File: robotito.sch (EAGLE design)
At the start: 53 parts, among them IC1 7805T, IC2 L298, IC3 L298, J1 22-27-2031-03, J10 22-27-2031-03, J11 22-27-2031-03, J2 22-27-2031-03, J3 22-27-2031-03, J4 22-27-2031-03, J5 22-27-2031-03, J6 22-27-2031-03, J7 22-27-2031-03, J8 22-27-2031-03, J9 22-27-2031-03

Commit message: Board is routing good with ~100 vias
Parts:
- removed U$1: TEENSY_3.1-3.2_DIL+4, Teensy_3_and_LC_Series_Boards_v1.4:TEENSY_3.1-3.2_DIL+4
- added J12: 22-27-2031-03, con-molex:22-27-2031-03
- added U$2: TEENSY_3.1-3.2_ALL_PINS&PADS, Teensy_3_and_LC_Series_Boards_v1.4:TEENSY_3.1-3.2_ALL_PINS&PADS
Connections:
- removed net N$33: U$1.AGND
- removed net N$34: U$1.AREF
- removed net N$36: U$1.VUSB
- removed net N$6: U$1.2
- new net DS12: J12-1.S
- new net N$15: U$2.31/A20
- new net N$4: U$2.2
- net +3.3V: now also U$2.3.3V; no longer U$1.3.3V
- net +5V: now also J12-3.S, U$2.VIN; no longer U$1.VIN
- net DS1: now also U$2.23/A9/T/PWM; no longer U$1.15/A1/T
- net DS10: now also U$2.29/A18/SCL1; no longer U$1.A11
- net DS11: now also U$2.30/A19/SDA1; no longer U$1.A10
- net DS2: now also U$2.A10; no longer U$1.16/A2/T
- net DS3: now also U$2.A11; no longer U$1.17/A3/T
- net DS4: now also U$2.A12; no longer U$1.18/A4/T/SDA0
- net DS5: now also U$2.A13; no longer U$1.19/A5/T/SCL0
- net DS6: now also U$2.A14/DAC; no longer U$1.20/A6/PWM
- net DS7: now also U$2.26/A15; no longer U$1.21/A7/PWM
- net DS8: now also U$2.27/A16; no longer U$1.22/A8/T/PWM
- net DS9: now also U$2.28/A17; no longer U$1.23/A9/T/PWM
- net GND: now also J12-2.S, U$2.GND; no longer U$1.GND
- net M1EN: now also U$2.3/CAN-TX/PWM; no longer U$1.3/CAN-TX/PWM
- net M1ENCA: now also U$2.15/A1/T
- net M1ENCB: now also U$2.16/A2/T
- net M1I1: now also U$2.7/RX3; no longer U$1.7/RX3
- net M1I2: now also U$2.8/TX3; no longer U$1.8/TX3
- net M2EN: now also U$2.4/CAN-RX/PWM; no longer U$1.4/CAN-RX-PWM
- net M2ENCA: now also U$2.17/A3/T
- net M2ENCB: now also U$2.18/A4/T/SDA0
- net M2I1: now also U$2.9/RX2/PWM; no longer U$1.9/RX2/PWM
- net M2I2: now also U$2.10/TX2/PWM; no longer U$1.10/TX2/PWM
- net M3EN: now also U$2.5/PWM; no longer U$1.5/PWM
- net M3ENCA: now also U$2.19/A5/T/SCL0
- net M3ENCB: now also U$2.20/A6/PWM
- net M3I1: now also U$2.11/MOSI; no longer U$1.11/MOSI
- net M3I2: now also U$2.12/MISO; no longer U$1.12/MISO
- net M4EN: now also U$2.6/PWM; no longer U$1.6/PWM
- net M4ENCA: now also U$2.21/A7/PWM
- net M4ENCB: now also U$2.22/A8/T/PWM
- net M4I1: now also U$2.13/SCK/LED; no longer U$1.13/SCK/LED
- net M4I2: now also U$2.14/A0; no longer U$1.14/A0
- net RX: now also U$2.0/RX1/T; no longer U$1.0/RX1/T
- net TX: now also U$2.1/TX1/T; no longer U$1.1/TX1/T

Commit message: fixed some errors/warnings
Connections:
- removed net CTS: JP1.CTS
- removed net DIO0: JP1.DIO0
- removed net DIO1: JP1.DIO1
- removed net DIO11: JP1.DIO11
- removed net DIO12: JP1.DIO12
- removed net DIO2: JP1.DIO2
- removed net DIO3: JP1.DIO3
- removed net DIO4: JP1.DIO4
- removed net DIO9: JP1.DIO9
- removed net DTR: JP1.DTR
- removed net N$1: D12.A, D4.A
- removed net N$15: U$2.31/A20
- removed net N$2: D16.A, D8.A
- removed net N$4: U$2.2
- removed net RES: JP1.RES@8
- removed net RES2: JP1.RES@14
- removed net RESET: JP1.RESET
- removed net RTS: JP1.RTS
- net DS12: now also U$2.31/A20
- net GND: now also D12.A, D16.A, D4.A, D8.A
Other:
- moved on the sheet: U$2

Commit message: juan and tj improvements draft
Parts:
- removed J1, J10, J11, J12, J2, J3, J4, J5, J6, J7, J8, J9: 22-27-2031-03, con-molex:22-27-2031-03
- removed SENSE1, SENSE2, SENSE3, SENSE4: .5, resistor:R-EU_0204/7
- added JP2, JP3: (no value), pinhead:PINHD-2X6
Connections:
- removed net N$10: IC2.SEN_A, SENSE1.1
- removed net N$11: IC2.SEN_B, SENSE2.1
- removed net N$3: IC3.SEN_A, SENSE3.1
- removed net N$8: IC3.SEN_B, SENSE4.1
- new net HB1GND: IC2.GND
- new net HB2GND: IC3.GND
- net +5V: now also IC2.VCC, IC3.VCC; no longer IC2.VS, IC3.VS, J1-3.S, J10-3.S, J11-3.S, J12-3.S, J2-3.S, J3-3.S, J4-3.S, J5-3.S, J6-3.S, J7-3.S, J8-3.S, J9-3.S
- net DS1: no longer J1-1.S
- net DS10: no longer J10-1.S
- net DS11: no longer J11-1.S
- net DS12: no longer J12-1.S
- net DS2: no longer J2-1.S
- net DS3: no longer J3-1.S
- net DS4: no longer J4-1.S
- net DS5: no longer J5-1.S
- net DS6: no longer J6-1.S
- net DS7: no longer J7-1.S
- net DS8: no longer J8-1.S
- net DS9: no longer J9-1.S
- net GND: now also IC2.SEN_A, IC2.SEN_B, IC3.SEN_A, IC3.SEN_B; no longer IC2.GND, IC3.GND, J1-2.S, J10-2.S, J11-2.S, J12-2.S, J2-2.S, J3-2.S, J4-2.S, J5-2.S, J6-2.S, J7-2.S, J8-2.S, J9-2.S, SENSE1.2, SENSE2.2, SENSE3.2, SENSE4.2
- net VCC: now also IC2.VS, IC3.VS; no longer IC2.VCC, IC3.VCC

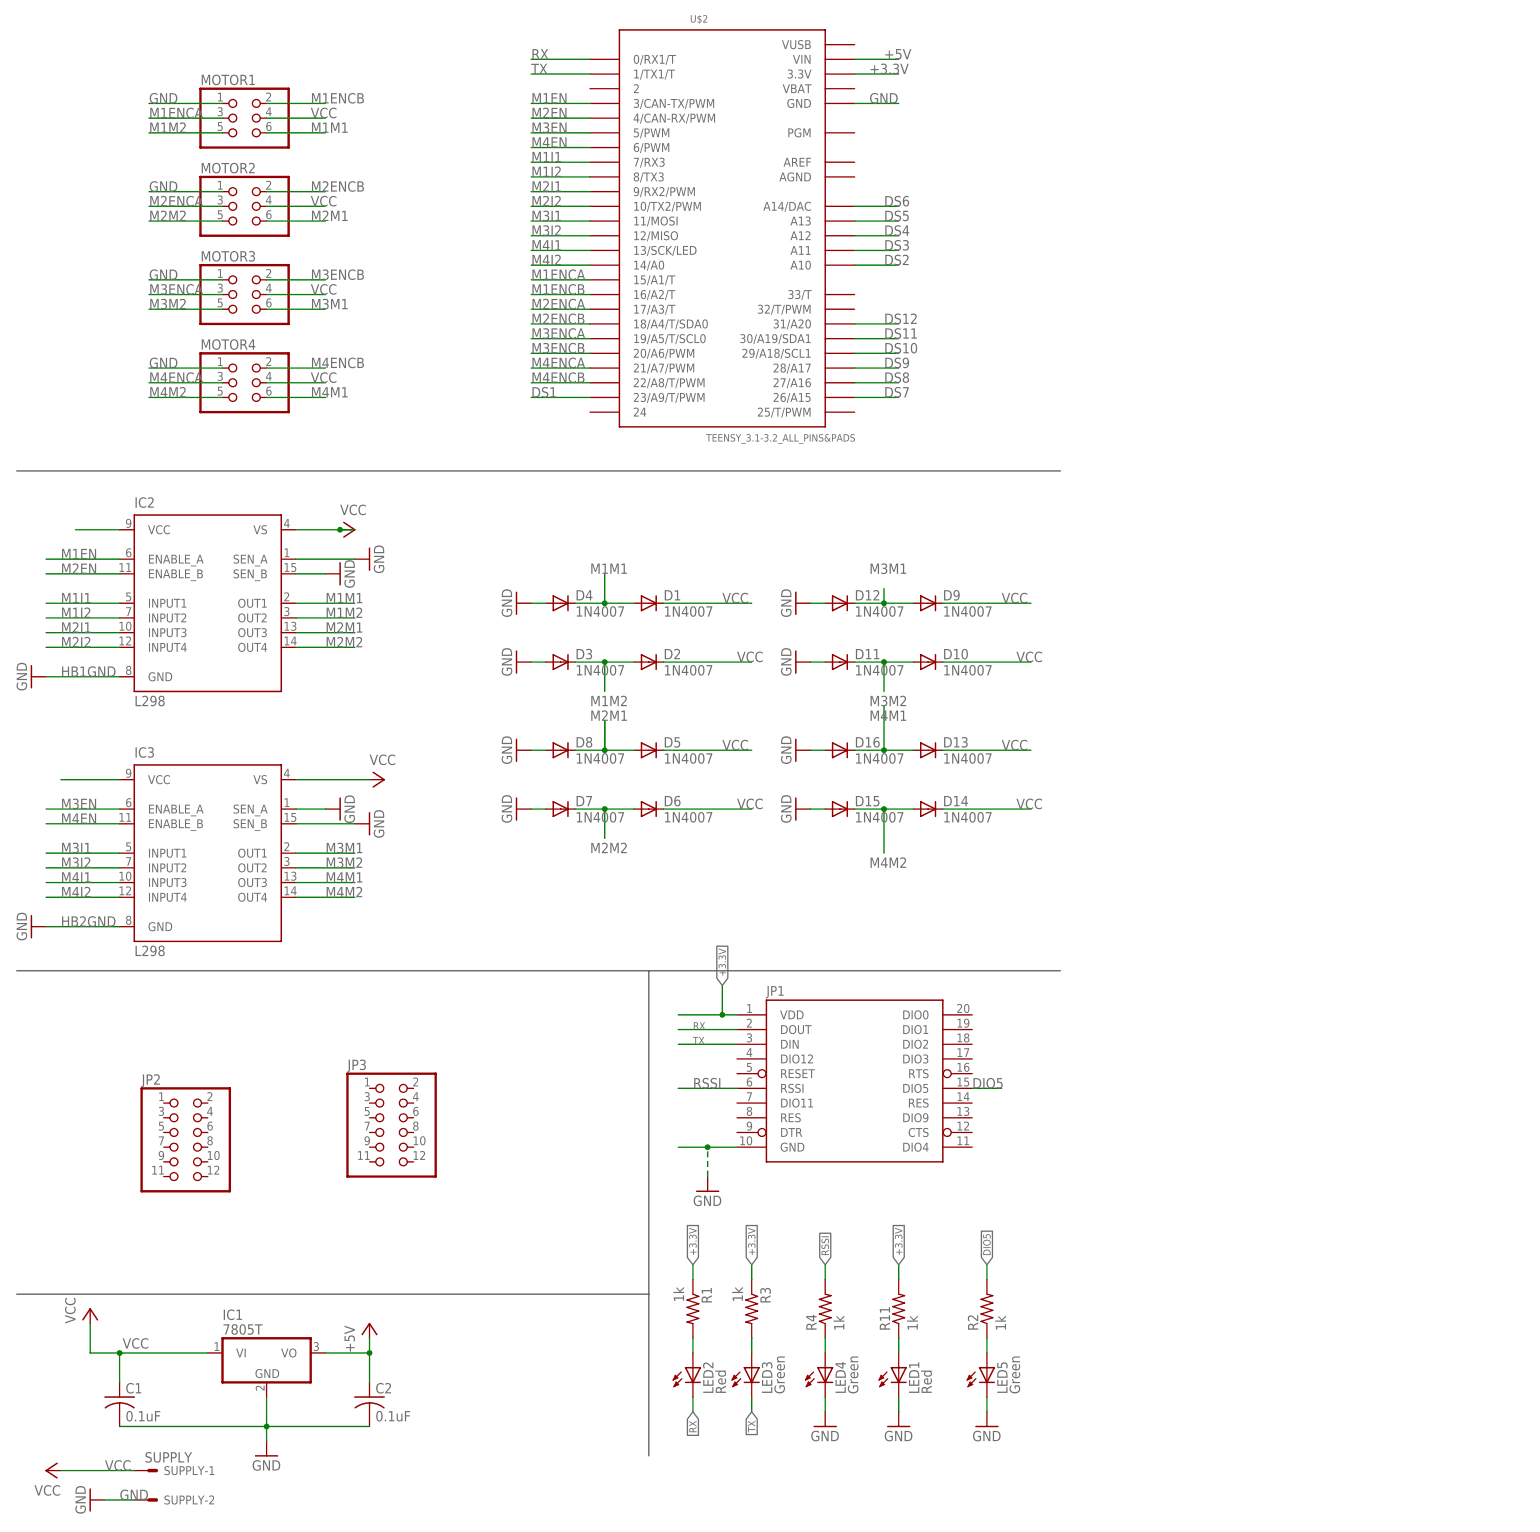
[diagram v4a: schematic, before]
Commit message: switch to powerso and .1 inch for sensors
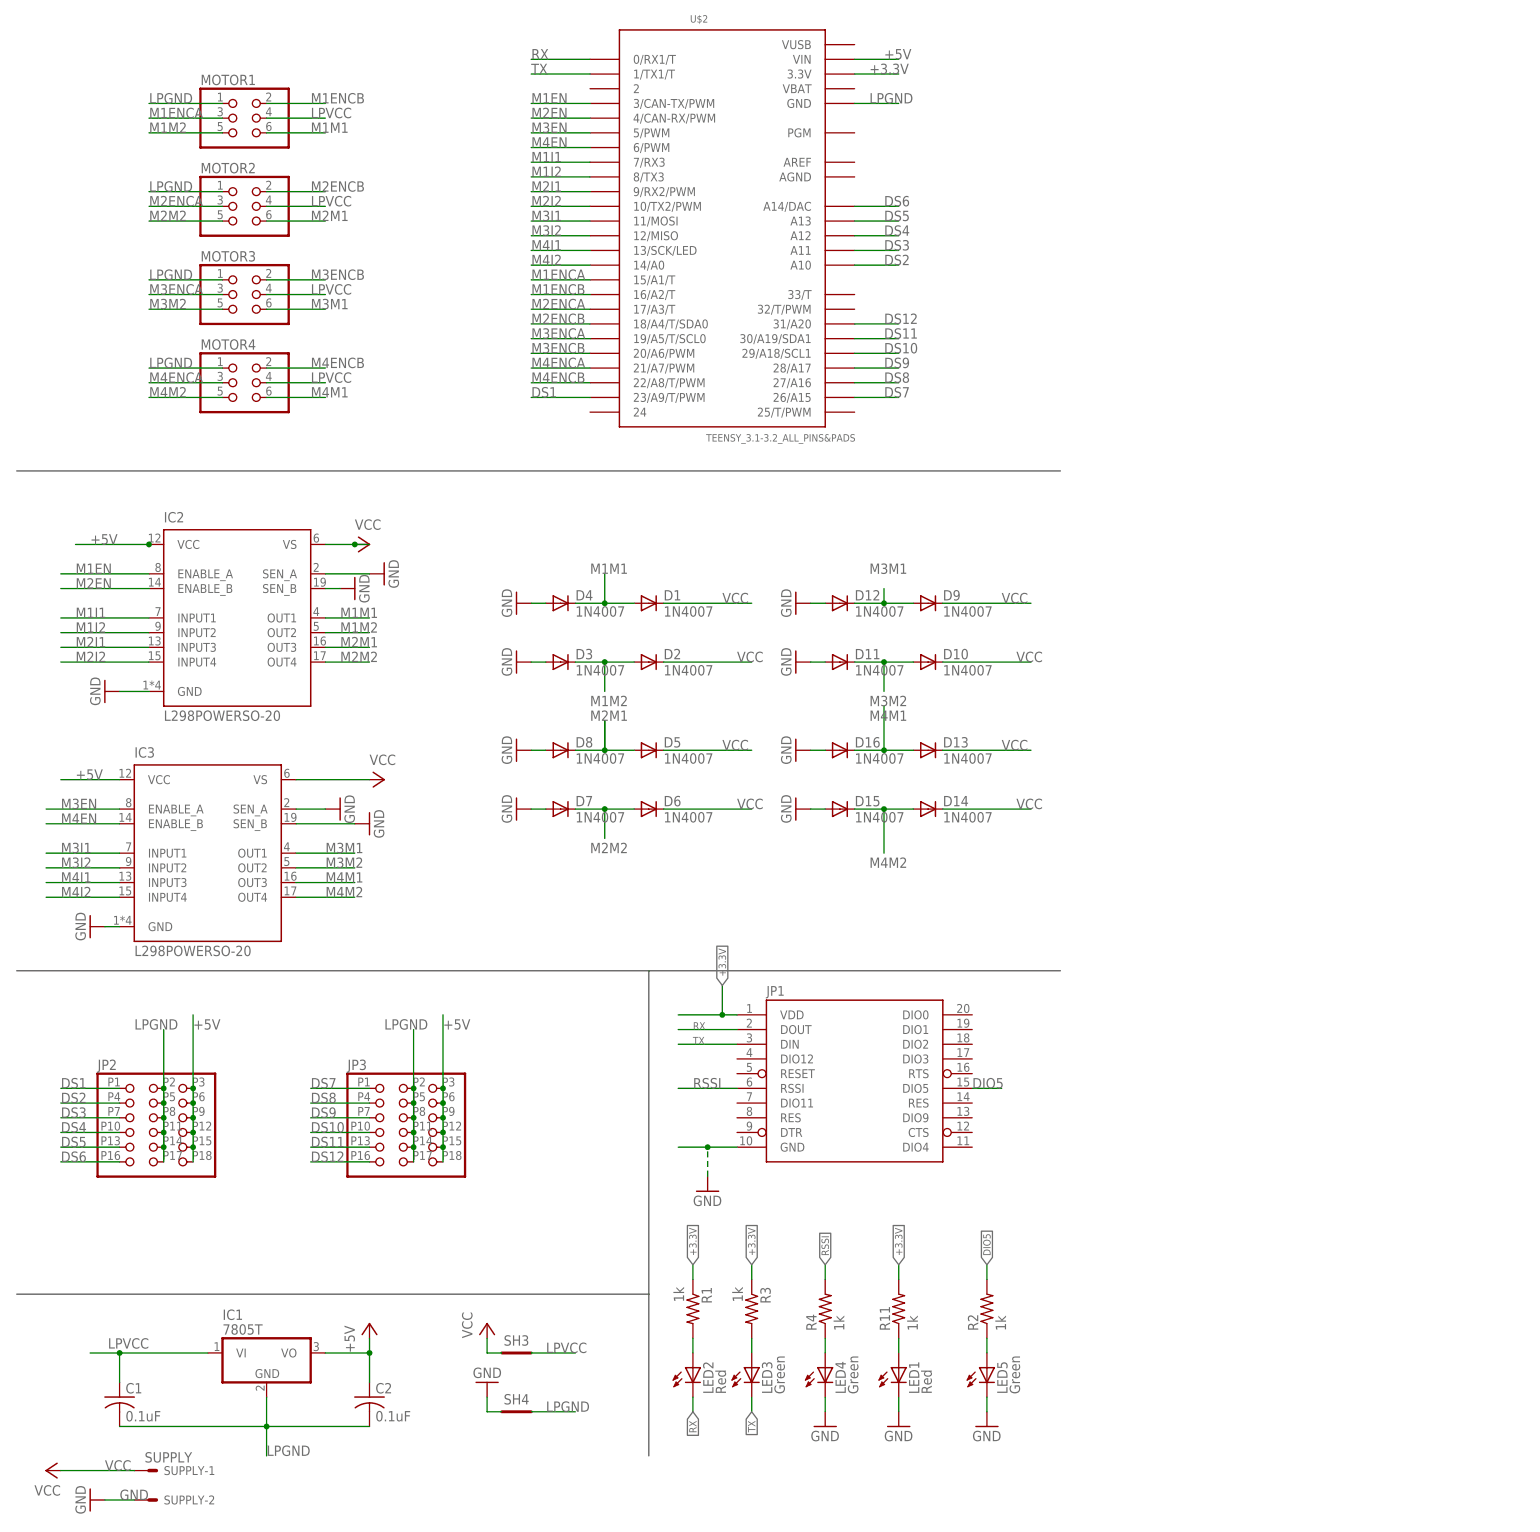
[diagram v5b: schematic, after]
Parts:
- added SH3, SH4: SHORT-HT5, shorts-old:SHORT-HT5
- IC2, IC3: value L298 -> L298POWERSO-20; device st-microelectronics:L298 -> mylibrary:L298POWERSO-20
- JP2, JP3: device pinhead:PINHD-2X6 -> mylibrary:PINHD-2X6
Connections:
- removed net HB1GND: IC2.GND
- removed net HB2GND: IC3.GND
- new net LPGND: C1.2, C2.2, IC1.GND, JP2.P11, JP2.P14, JP2.P17, JP2.P2, JP2.P5, JP2.P8, JP3.P11, JP3.P14, JP3.P17, JP3.P2, JP3.P5, JP3.P8, MOTOR1.1, MOTOR2.1, MOTOR3.1, MOTOR4.1, SH4.P$2, U$2.GND
- new net LPVCC: C1.1, IC1.VI, MOTOR1.4, MOTOR2.4, MOTOR3.4, MOTOR4.4, SH3.P$2
- net +5V: now also JP2.P12, JP2.P15, JP2.P18, JP2.P3, JP2.P6, JP2.P9, JP3.P12, JP3.P15, JP3.P18, JP3.P3, JP3.P6, JP3.P9
- net DS1: now also JP2.P1
- net DS10: now also JP3.P10
- net DS11: now also JP3.P13
- net DS12: now also JP3.P16
- net DS2: now also JP2.P4
- net DS3: now also JP2.P7
- net DS4: now also JP2.P10
- net DS5: now also JP2.P13
- net DS6: now also JP2.P16
- net DS7: now also JP3.P1
- net DS8: now also JP3.P4
- net DS9: now also JP3.P7
- net GND: now also IC2.GND, IC3.GND, SH4.P$1; no longer C1.2, C2.2, IC1.GND, MOTOR1.1, MOTOR2.1, MOTOR3.1, MOTOR4.1, U$2.GND
- net VCC: now also SH3.P$1; no longer C1.1, IC1.VI, MOTOR1.4, MOTOR2.4, MOTOR3.4, MOTOR4.4
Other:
- moved on the sheet: IC2, IC3

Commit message: Fix separation to comply with pcbway. V1 sent to print
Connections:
- net +5V: now also JP2.P11, JP2.P14, JP2.P17, JP2.P2, JP2.P5, JP2.P8, JP3.P11, JP3.P14, JP3.P17, JP3.P2, JP3.P5, JP3.P8; no longer JP2.P12, JP2.P15, JP2.P18, JP2.P3, JP2.P6, JP2.P9, JP3.P12, JP3.P15, JP3.P18, JP3.P3, JP3.P6, JP3.P9
- net LPGND: now also JP2.P12, JP2.P15, JP2.P18, JP2.P3, JP2.P6, JP2.P9, JP3.P12, JP3.P15, JP3.P18, JP3.P3, JP3.P6, JP3.P9; no longer JP2.P11, JP2.P14, JP2.P17, JP2.P2, JP2.P5, JP2.P8, JP3.P11, JP3.P14, JP3.P17, JP3.P2, JP3.P5, JP3.P8
